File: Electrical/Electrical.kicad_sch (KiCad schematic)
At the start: 13 parts, among them P1 USB_C_Plug_USB2.0, U1 AP2112K-3.3

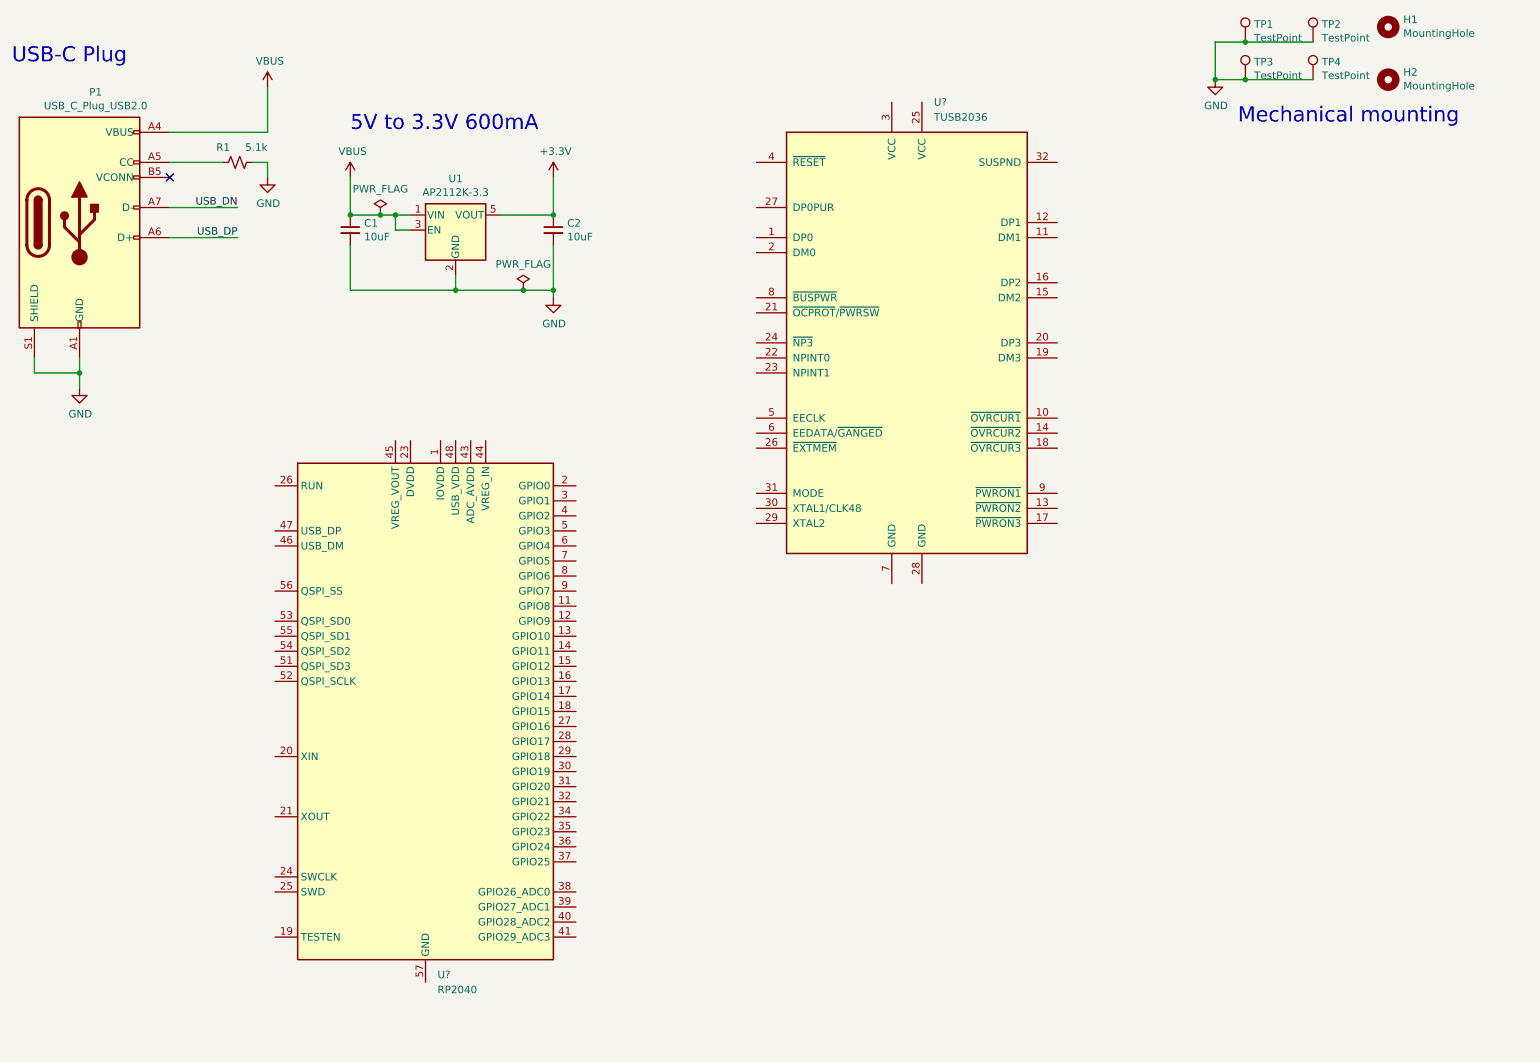
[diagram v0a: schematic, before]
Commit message: removed USB hub
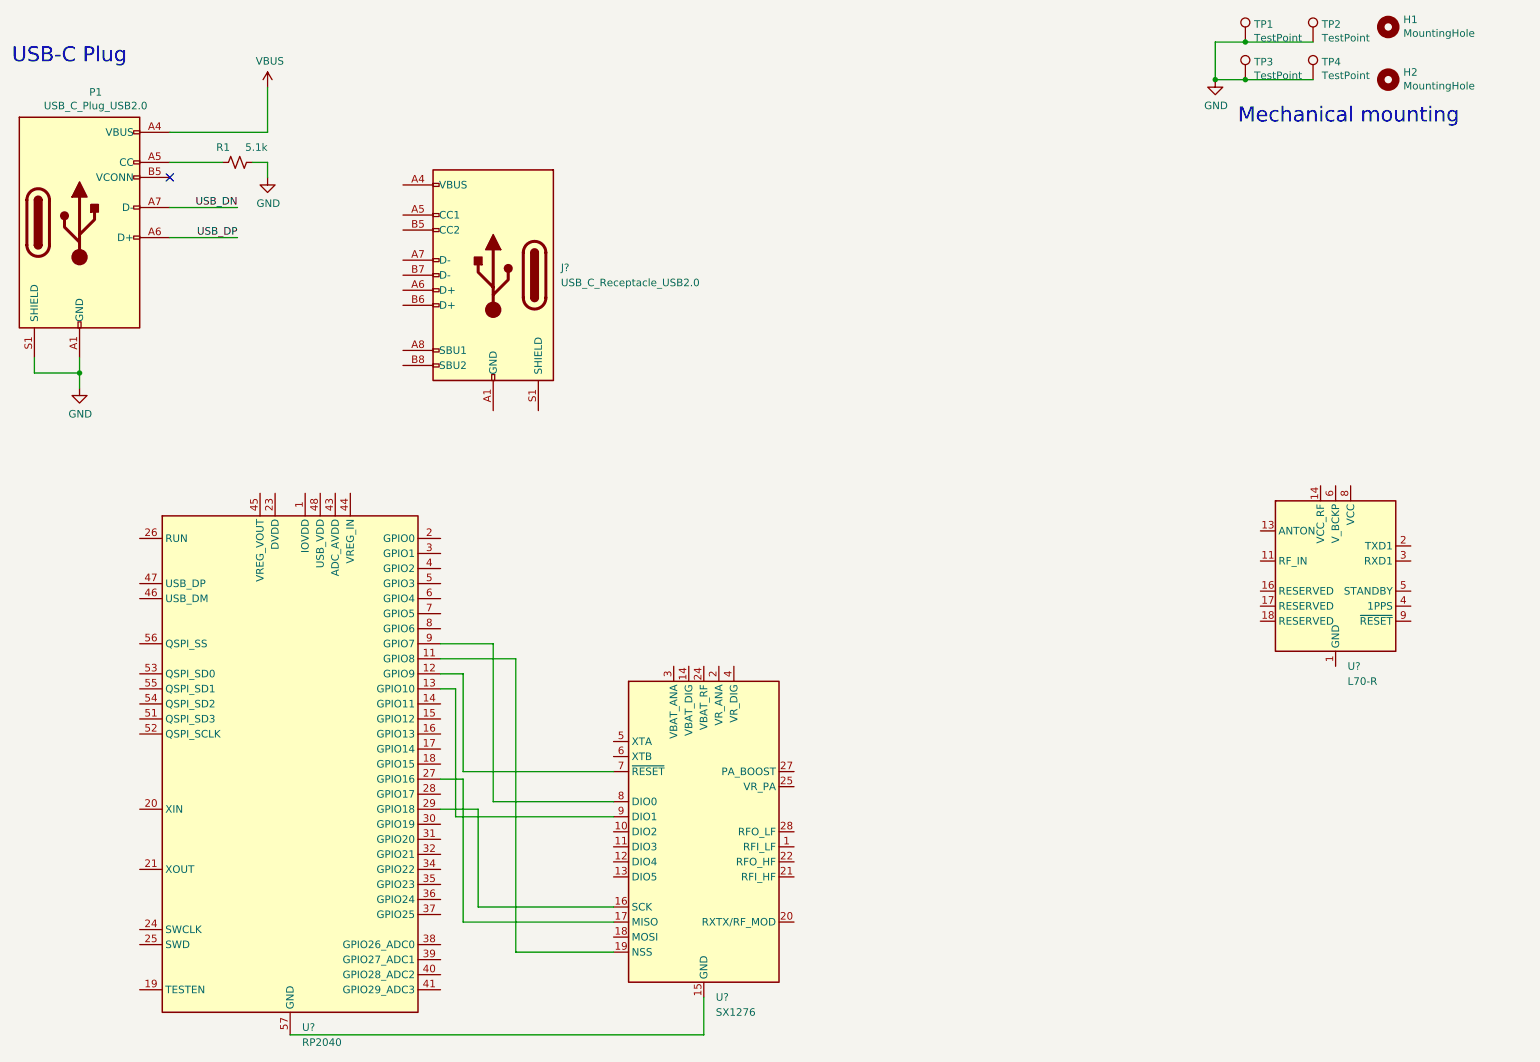
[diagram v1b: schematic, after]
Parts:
- removed C1, C2: 10uF, Capacitor_SMD:C_0805_2012Metric, symbol Device:C_Small
- removed U1: AP2112K-3.3, Package_TO_SOT_SMD:SOT-23-5, symbol Regulator_Linear:AP2112K-3.3
- removed U?: TUSB2036, Package_QFP:LQFP-32_7x7mm_P0.8mm, symbol Interface_USB:TUSB2036
- added J?: USB_C_Receptacle_USB2.0, Connector_USB:USB_C_Receptacle_HRO_TYPE-C-31-M-12, symbol Connector:USB_C_Receptacle_USB2.0
- added U?: L70-R, RF_GPS:Quectel_L70-R, symbol RF_GPS:L70-R
- added U?: SX1276, Package_DFN_QFN:QFN-28-1EP_6x6mm_P0.65mm_EP4.8x4.8mm, symbol RF:SX1276
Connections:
- net at U?.11 (GPIO8): now also U?.19 (NSS)
- net at U?.12 (GPIO9): now also U?.7 (~{RESET})
- net at U?.13 (GPIO10): now also U?.9 (DIO1)
- net at U?.27 (GPIO16): now also U?.17 (MISO)
- net at U?.29 (GPIO18): now also U?.16 (SCK)
- net at U?.57 (GND): now also U?.15 (GND), U?.23 (GND), U?.26 (GND), U?.29 (GND)
- net at U?.9 (GPIO7): now also U?.8 (DIO0)
- new net: J?.A1 (GND), J?.A12 (GND), J?.B1 (GND), J?.B12 (GND)
- new net: J?.A4 (VBUS), J?.A9 (VBUS), J?.B4 (VBUS), J?.B9 (VBUS)
- new net: U?.1 (GND), U?.10 (GND), U?.12 (GND)
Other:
- note removed: "5V to 3.3V 600mA"
- moved on the sheet: U?
